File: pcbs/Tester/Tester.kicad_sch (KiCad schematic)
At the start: 0 parts

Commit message: Lots of rethinking
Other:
- sheet Out Registers ports: added ~{OE[1..5]}; removed none
- sheet Pi Input ports: added ~{OE[1..5]}; removed none

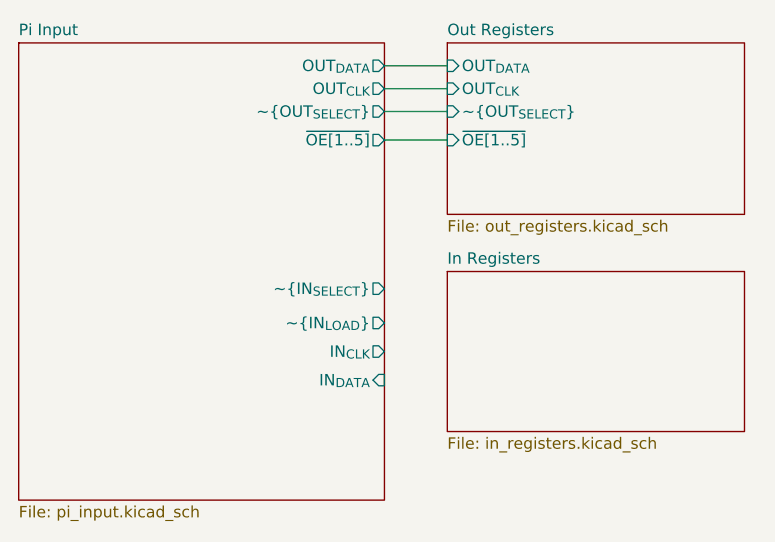
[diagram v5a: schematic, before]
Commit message: Turn those transceivers the other way up
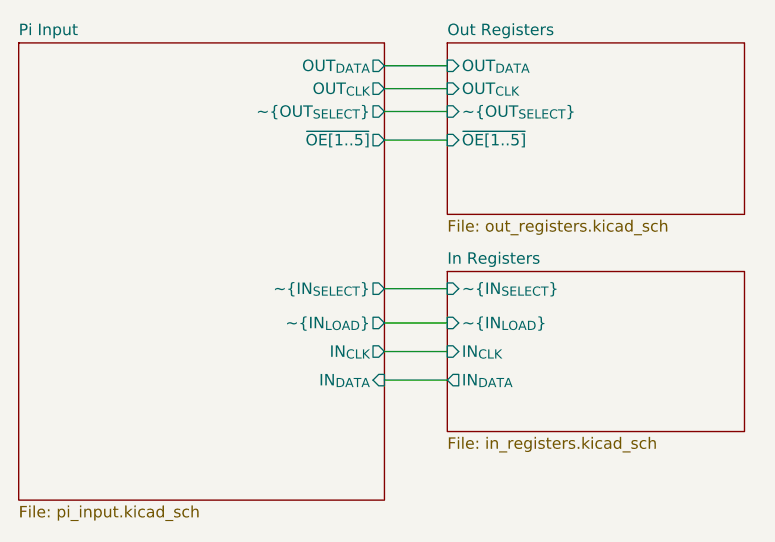
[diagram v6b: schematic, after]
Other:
- sheet In Registers ports: added IN_{CLK}, IN_{DATA}, ~{IN_{LOAD}}, ~{IN_{SELECT}}; removed none
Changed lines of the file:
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@@
+    (stroke (width 0) (type default) (color 0 0 0 0))
+  )
+  (wire (pts (xy 69.215 71.755) (xy 76.2 71.755))
+    (stroke (width 0) (type default) (color 0 0 0 0))
+  )
+  (wire (pts (xy 69.215 81.915) (xy 76.2 81.915))
     (stroke (width 0) (type default) (color 0 0 0 0))
   )
   (wire (pts (xy 69.215 55.245) (xy 76.2 55.245))
+    (stroke (width 0) (type default) (color 0 0 0 0))
+  )
+  (wire (pts (xy 69.215 75.565) (xy 76.2 75.565))
+    (stroke (width 0) (type default) (color 0 0 0 0))
+  )
+  (wire (pts (xy 69.215 78.74) (xy 76.2 78.74))
     (stroke (width 0) (type default) (color 0 0 0 0))
   )
@@
       (effects (font (size 1.27 1.27)) (justify left top))
     )
+    (pin "IN_{CLK}" input (at 76.2 78.74 180)
+      (effects (font (size 1.27 1.27)) (justify left))
+    )
+    (pin "~{IN_{SELECT}}" input (at 76.2 71.755 180)
+      (effects (font (size 1.27 1.27)) (justify left))
+    )
+    (pin "~{IN_{LOAD}}" input (at 76.2 75.565 180)
+      (effects (font (size 1.27 1.27)) (justify left))
+    )
+    (pin "IN_{DATA}" output (at 76.2 81.915 180)
+      (effects (font (size 1.27 1.27)) (justify left))
+    )
   )
   (sheet_instances
@@
       (reference "#PWR0206") (unit 1) (value "GND") (footprint "")
     )
+    (path "/53be72d8-80b1-4e19-9ce6-cadb107d3874/ec9940a2-b675-4bda-b3ae-13bafa9b0617"
+      (reference "#PWR0207") (unit 1) (value "+5V") (footprint "")
+    )
     (path "/53be72d8-80b1-4e19-9ce6-cadb107d3874/c6c38a78-045e-411c-bbc5-38cd6ce39d3c"
       (reference "#PWR0208") (unit 1) (value "GND") (footprint "")
     )
+    (path "/53be72d8-80b1-4e19-9ce6-cadb107d3874/15156c95-b465-4b29-99b1-7a0a2600627e"
+      (reference "#PWR0209") (unit 1) (value "GND") (footprint "")
+    )
     (path "/53be72d8-80b1-4e19-9ce6-cadb107d3874/5c4719c1-c053-4d28-a16e-e31d8caf645c"
       (reference "#PWR0210") (unit 1) (value "+5V") (footprint "")
@@
       (reference "#PWR0220") (unit 1) (value "+3V3") (footprint "")
     )
+    (path "/53be72d8-80b1-4e19-9ce6-cadb107d3874/bd1a0c2a-2c8f-4a17-a161-7b88e88a6335"
+      (reference "#PWR0221") (unit 1) (value "+5V") (footprint "")
+    )
+    (path "/53be72d8-80b1-4e19-9ce6-cadb107d3874/1a15746c-1ec4-4944-93e3-b66001c25b21"
+      (reference "#PWR0222") (unit 1) (value "GND") (footprint "")
+    )
     (path "/a8002812-6b05-4e18-8452-6d0cfe03608a/47a48205-a6d3-4801-9864-fc6e5d30d5bf"
       (reference "#PWR0301") (unit 1) (value "+5V") (footprint "")
@@
       (reference "#PWR0416") (unit 1) (value "GND") (footprint "")
     )
+    (path "/53be72d8-80b1-4e19-9ce6-cadb107d3874/6b8ca05a-4450-4a52-9ba7-56d25d563f6e"
+      (reference "C201") (unit 1) (value "100n") (footprint "Capacitor_SMD:C_0603_1608Metric")
+    )
+    (path "/53be72d8-80b1-4e19-9ce6-cadb107d3874/7d94493d-27b8-4821-8ea2-90e83e0868ce"
+      (reference "C202") (unit 1) (value "100n") (footprint "Capacitor_SMD:C_0603_1608Metric")
+    )
+    (path "/53be72d8-80b1-4e19-9ce6-cadb107d3874/0fa923fa-2974-4e2b-bfb9-a583c295fb23"
+      (reference "C203") (unit 1) (value "100n") (footprint "Capacitor_SMD:C_0603_1608Metric")
+    )
     (path "/a8002812-6b05-4e18-8452-6d0cfe03608a/ede43bda-6227-4899-9694-af731d4fa471"
       (reference "C301") (unit 1) (value "100n") (footprint "Capacitor_SMD:C_0603_1608Metric")
@@
       (reference "J201") (unit 1) (value "Raspberry_Pi_2_3") (footprint "Connector_PinHeader_2.54mm:PinHeader_2x20_P2.54mm_Vertical")
     )
+    (path "/53be72d8-80b1-4e19-9ce6-cadb107d3874/3e879c5a-ceb0-4b76-9d05-ec7517885256"
+      (reference "J202") (unit 1) (value "Conn_01x04") (footprint "Connector_PinHeader_2.54mm:PinHeader_1x04_P2.54mm_Vertical")
+    )
     (path "/a8002812-6b05-4e18-8452-6d0cfe03608a/e49144d7-c420-42f7-8673-ddafe8b2c59c"
